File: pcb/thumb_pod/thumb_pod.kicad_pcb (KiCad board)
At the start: 2 copper layers, 60 x 56 mm, 17 parts, among them J1 Conn_02x06_Odd_Even, SW1 SW_Push, SW2 SW_Push, SW3 SW_Push, SW4 SW_Push, U1 RKJXM1015004

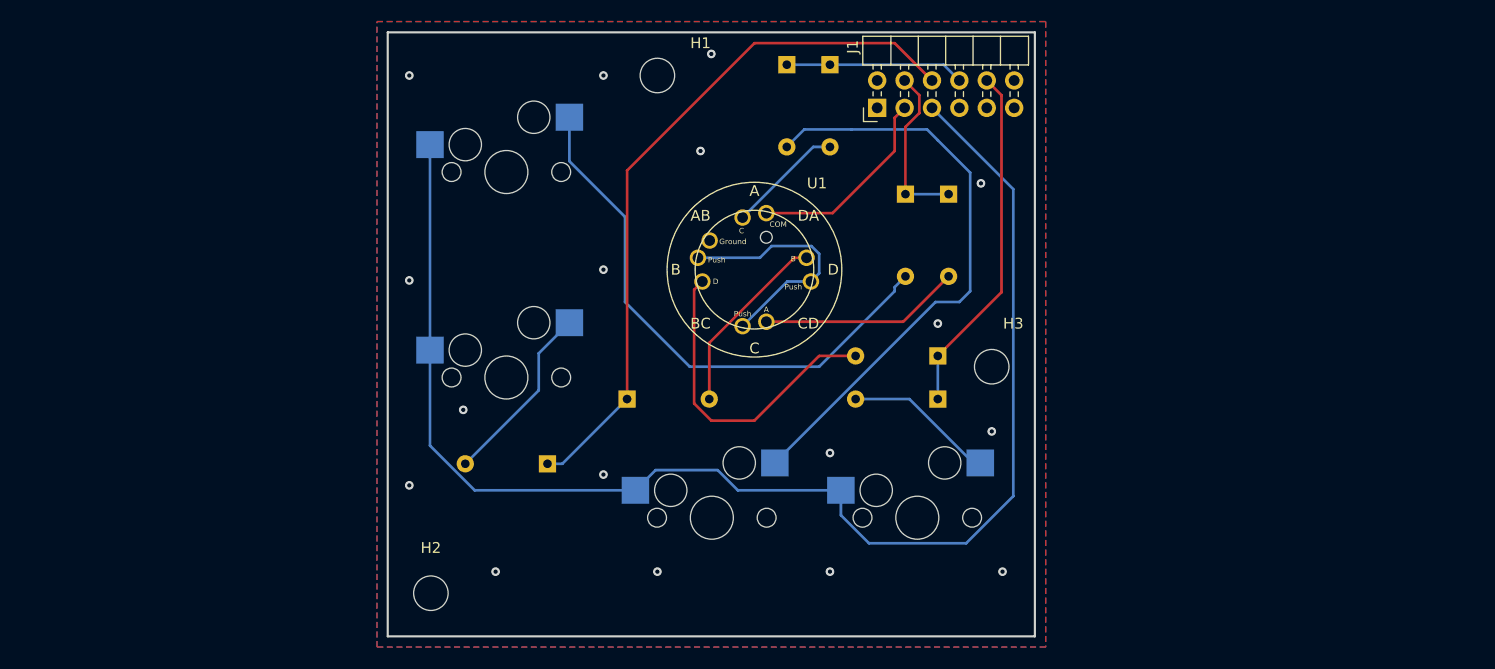
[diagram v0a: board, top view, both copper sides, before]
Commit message: - Added multiple positions for each switch to allow for tweaking
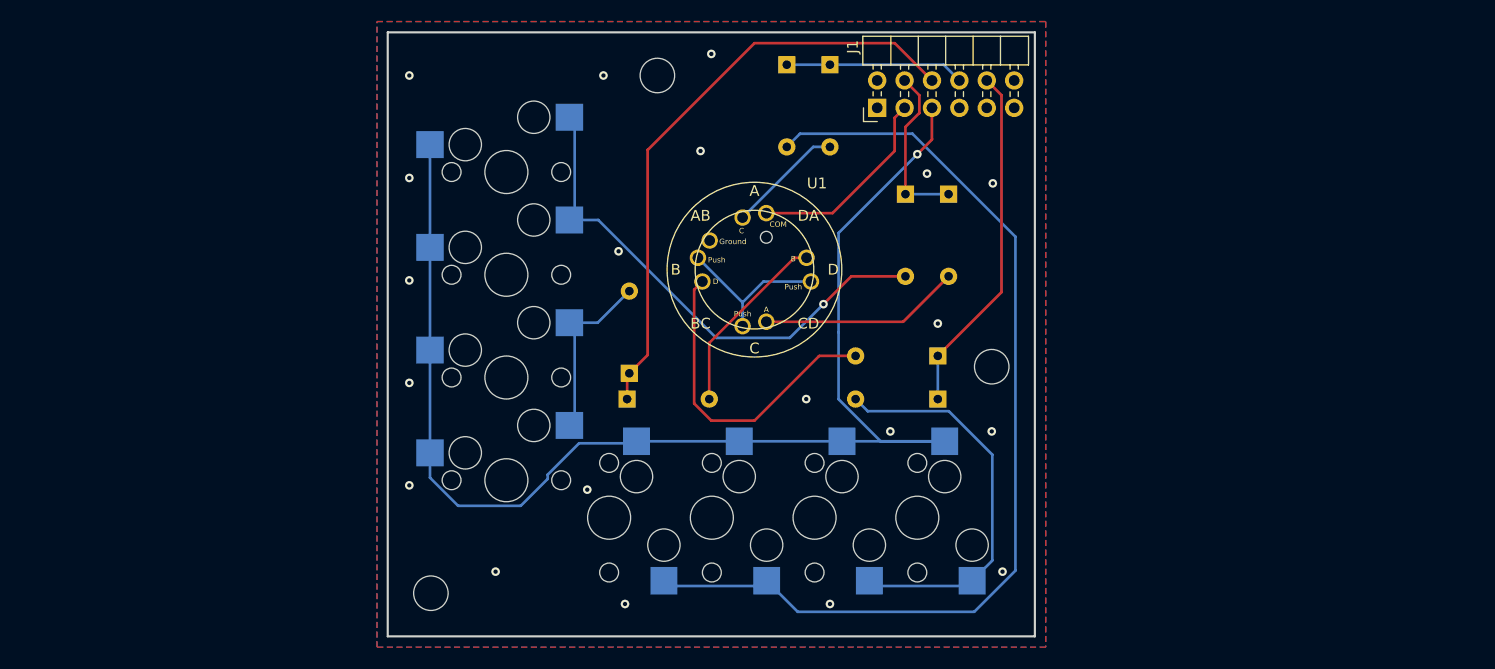
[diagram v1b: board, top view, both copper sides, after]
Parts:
- added SW5: SW_Push, keypad:MXOnly-1U-Hotswap, F.Cu at (97.0, 46.5)
- added SW6: SW_Push, keypad:MXOnly-1U-Hotswap, F.Cu at (97.0, 65.5)
- added SW7: SW_Push, keypad:MXOnly-1U-Hotswap, F.Cu at (106.5, 69.0)
- added SW8: SW_Push, keypad:MXOnly-1U-Hotswap, F.Cu at (125.6, 69.0)
- moved D4 11.3 mm to (108.4, 55.6), turned to 90 degrees
- turned SW3 to -90 degrees
- turned SW4 to -90 degrees
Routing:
- net Net-(D6-Pad2): track 55.0 -> 92.4 mm
- net Net-(D8-Pad2): track 14.0 -> 37.2 mm
- net /Col1: track 65.7 -> 55.8 mm
- net unconnected-(U1-Pad3): track 22.9 -> 15.5 mm
- net /Row5: track 129.6 -> 124.4 mm, vias 0 -> 1
- net Net-(SW1-Pad2): track 51.4 -> 48.0 mm, vias 0 -> 1
- net /GND: vias 17 -> 20

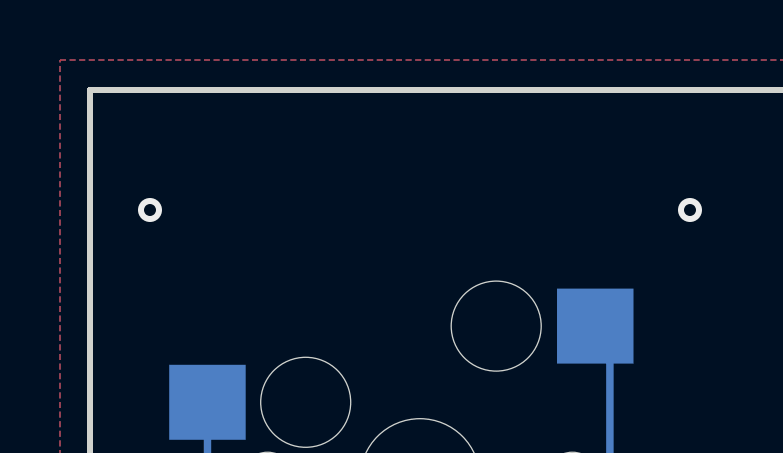
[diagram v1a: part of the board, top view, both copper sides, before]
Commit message: - Added a board label and version
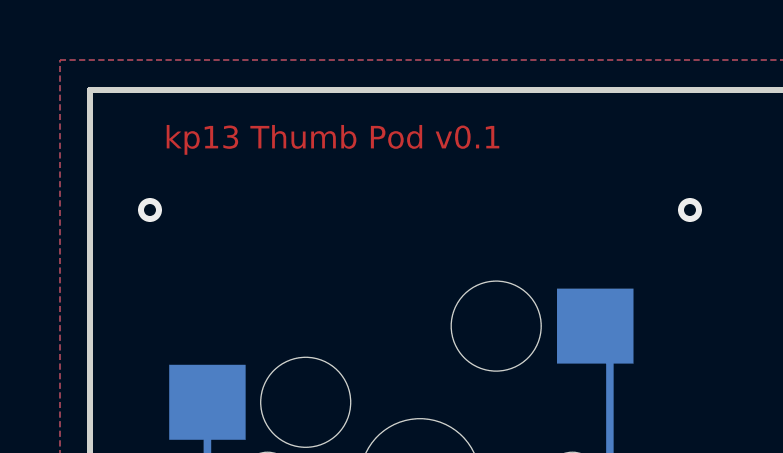
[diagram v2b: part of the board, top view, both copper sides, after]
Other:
- board text added: "kp13 Thumb Pod v0.1"
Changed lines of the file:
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@@
   (gr_line (start 146 24) (end 86 24) (layer "Edge.Cuts") (width 0.2))
   (gr_line (start 86 80) (end 146 80) (layer "Edge.Cuts") (width 0.2))
+  (gr_text "kp13 Thumb Pod v0.1" (at 94.1 25.6) (layer "F.Cu")
+    (effects (font (size 0.75 0.75) (thickness 0.1875)))
+  )
   (segment (start 135.285 29.825) (end 135.285 31.486701) (width 0.25) (layer "F.Cu") (net 1))
   (segment (start 135.285 31.486701) (end 134 32.771701) (width 0.25) (layer "F.Cu") (net 1))

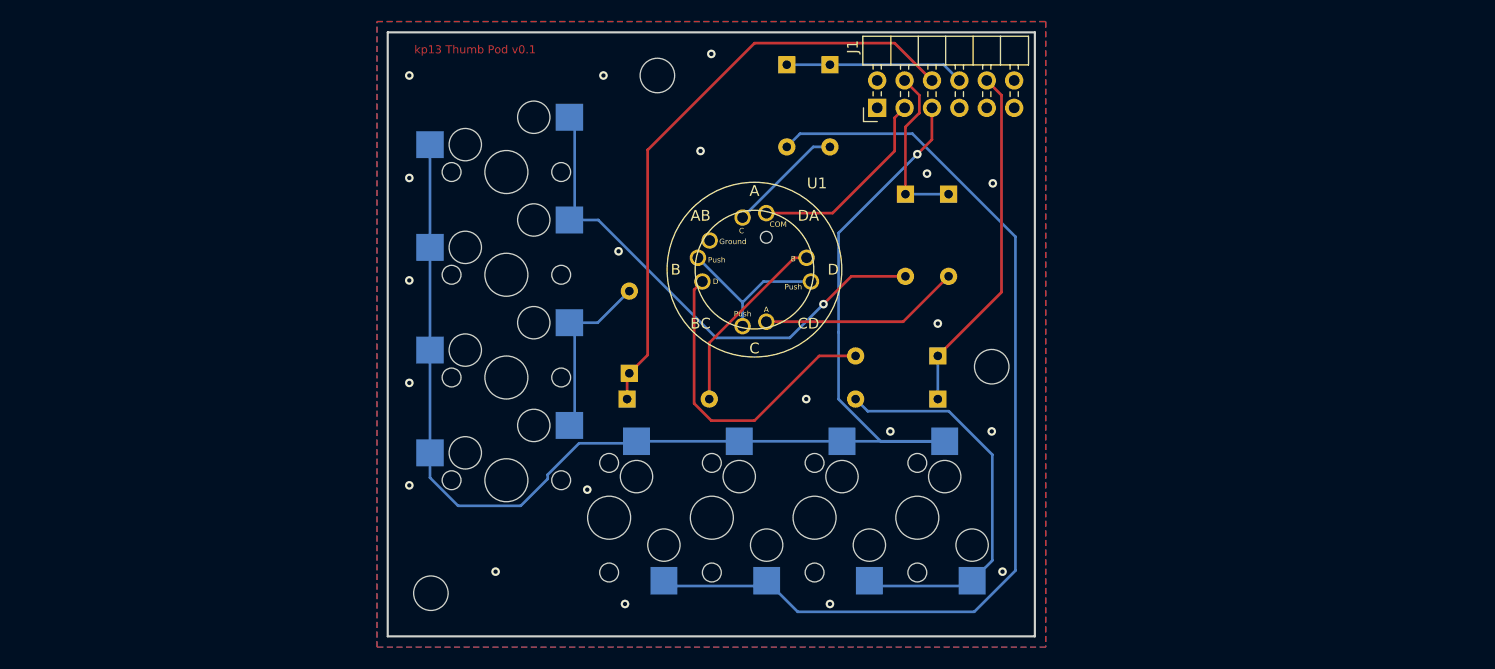
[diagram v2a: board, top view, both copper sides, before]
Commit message: - Added a preliminary "mini" thumb pod with only the directional stick  - Added mouse bite footprint from Panelization.pretty
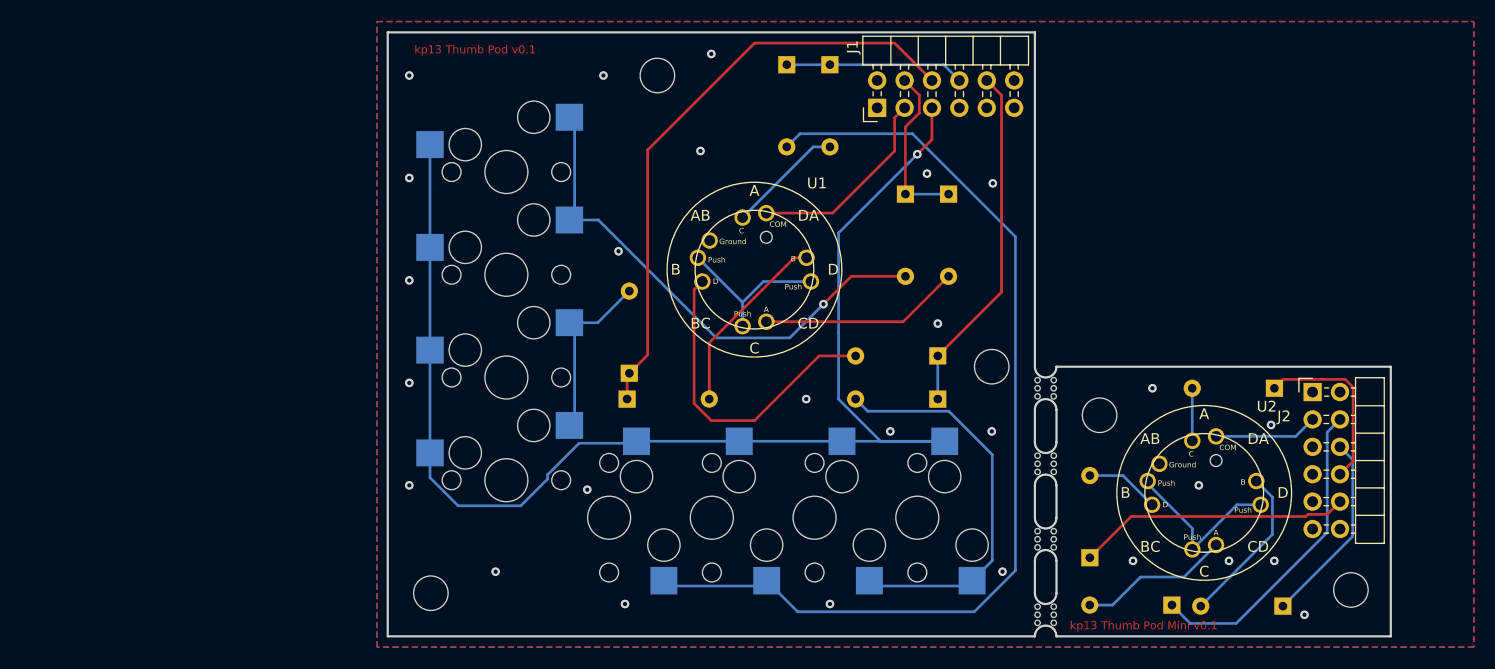
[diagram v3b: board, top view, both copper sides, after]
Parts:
- added D10: 1N4148, Diode_THT:D_DO-35_SOD27_P7.62mm_Horizontal, B.Cu at (169.0, 77.2)
- added D11: 1N4148, Diode_THT:D_DO-35_SOD27_P7.62mm_Horizontal, B.Cu at (168.2, 57.0)
- added D12: 1N4148, Diode_THT:D_DO-35_SOD27_P7.62mm_Horizontal, B.Cu at (151.1, 72.7)
- added D9: 1N4148, Diode_THT:D_DO-35_SOD27_P7.62mm_Horizontal, B.Cu at (158.7, 77.1)
- added H4: MountingHole, MountingHole:MountingHole_3.2mm_M3, F.Cu at (152.0, 59.5)
- added H5: MountingHole, MountingHole:MountingHole_3.2mm_M3, F.Cu at (175.3, 75.7)
- added J2: Conn_02x06_Odd_Even, keypad:PinHeader_2x06_P2.54mm_Horizontal, F.Cu at (171.8, 57.4)
- added U2: RKJXM1015004, thumb_pod:RKJXM1015004, F.Cu at (161.7, 66.7)
- added mouse-bite-2mm-slot: VAL**, thumb_pod:mouse-bite-2mm-slot, F.Cu at (147.0, 78.0)
- added mouse-bite-2mm-slot: VAL**, thumb_pod:mouse-bite-2mm-slot, F.Cu at (147.0, 64.0)
- added mouse-bite-2mm-slot: VAL**, thumb_pod:mouse-bite-2mm-slot, F.Cu at (147.0, 71.0)
- added mouse-bite-2mm-slot: VAL**, thumb_pod:mouse-bite-2mm-slot, F.Cu at (147.0, 57.0)
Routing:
- net /Col0: track 15.6 -> 45.2 mm
- net /Col3: track 32.6 -> 57.9 mm
- net /Col1: track 55.8 -> 73.7 mm
- net /Col2: track 16.6 -> 33.1 mm
- net unconnected-(U2-Pad3): track 0.00 -> 16.1 mm
- net Net-(D10-Pad2): track 0.00 -> 15.0 mm
- net Net-(D9-Pad2): track 0.00 -> 14.0 mm
- net /Row4: track 18.7 -> 28.3 mm
- net Net-(D12-Pad2): track 0.00 -> 6.89 mm
- net Net-(D11-Pad2): track 0.00 -> 4.87 mm
- net /GND: vias 20 -> 27
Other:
- board size 60 x 56 mm -> 93 x 56 mm
- board text added: "kp13 Thumb Pod Mini v0.1"

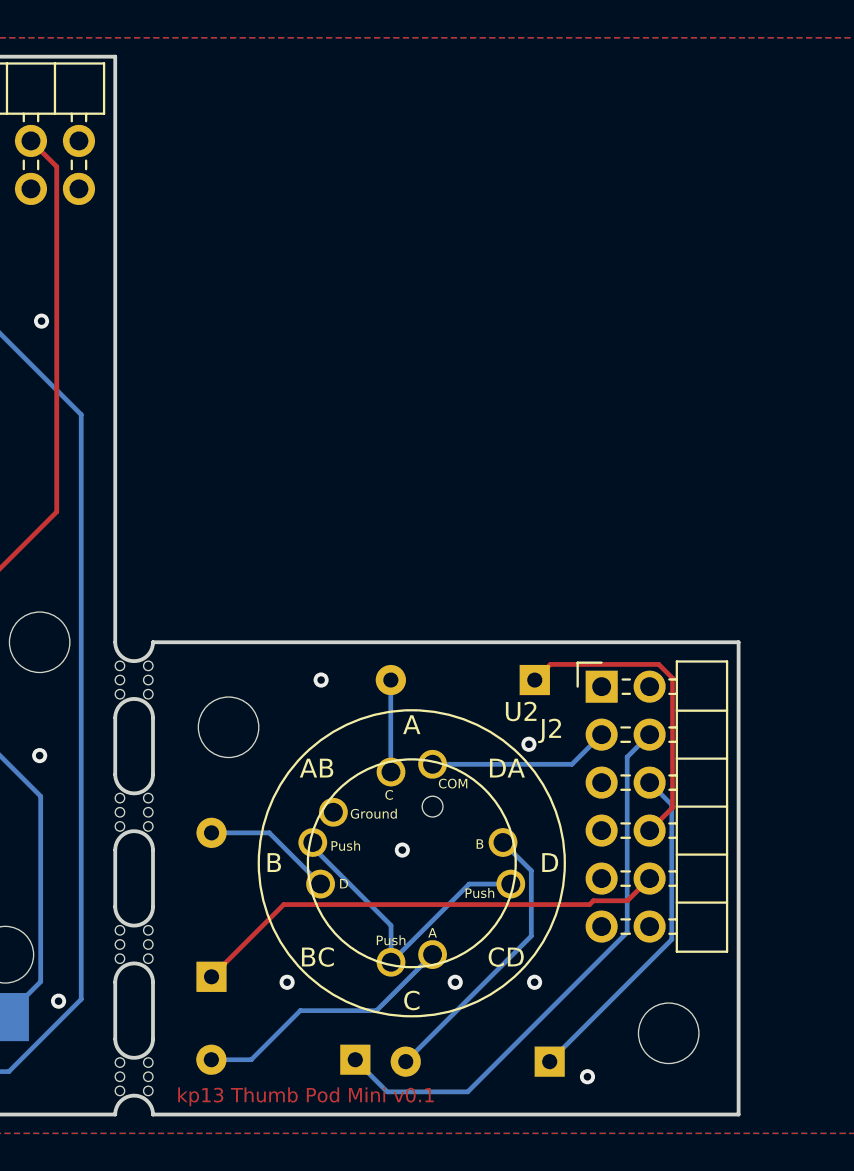
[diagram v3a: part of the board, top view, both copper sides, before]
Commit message: - Added experimental alternate layouts for the thumb pod  - Attempted some DIY panelization
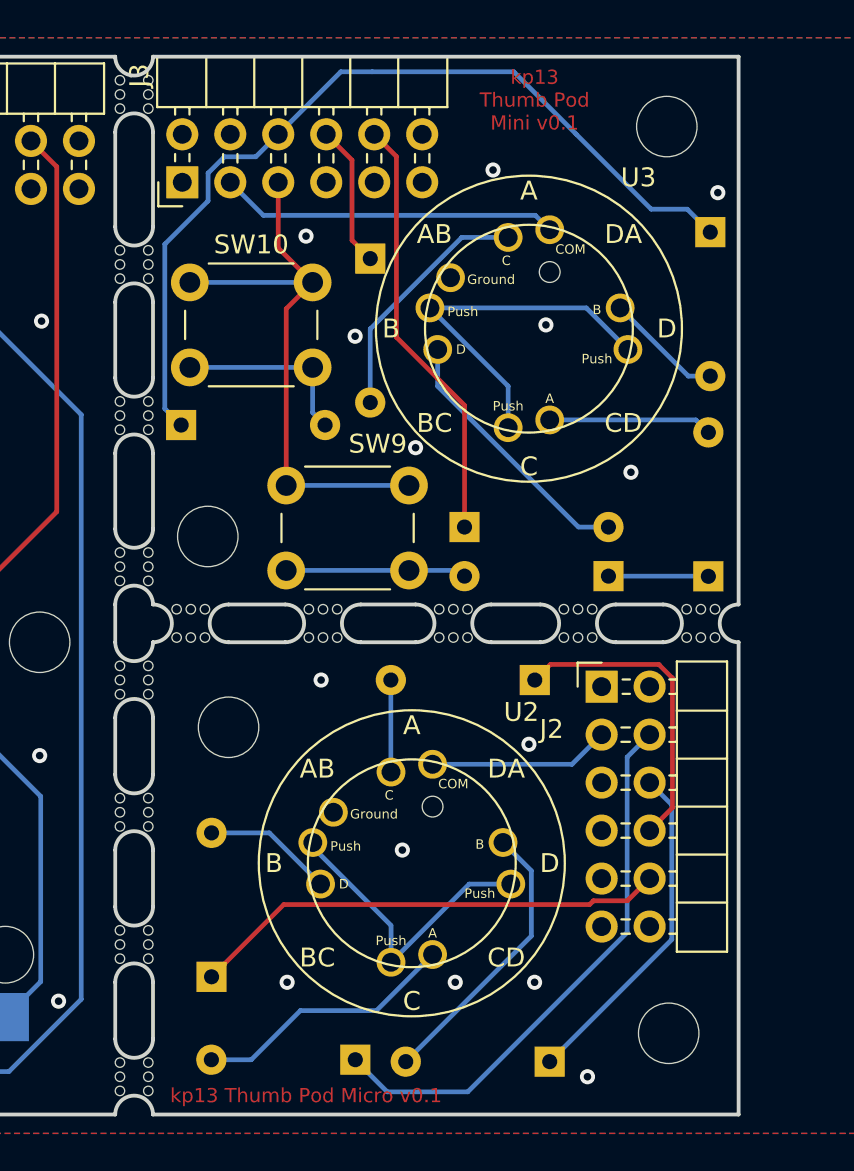
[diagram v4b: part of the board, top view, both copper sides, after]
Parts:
- added D13: 1N4148, Diode_THT:D_DO-35_SOD27_P7.62mm_Horizontal, B.Cu at (177.4, 51.5)
- added D14: 1N4148, Diode_THT:D_DO-35_SOD27_P7.62mm_Horizontal, B.Cu at (177.5, 33.3)
- added D15: 1N4148, Diode_THT:D_DO-35_SOD27_P7.62mm_Horizontal, B.Cu at (159.5, 34.7)
- added D16: 1N4148, Diode_THT:D_DO-35_SOD27_P7.62mm_Horizontal, B.Cu at (172.1, 51.5)
- added D17: 1N4148, Diode_THT:D_DO-35_SOD27_P7.62mm_Horizontal, B.Cu at (164.5, 48.9)
- added D18: 1N4148, Diode_THT:D_DO-35_SOD27_P7.62mm_Horizontal, B.Cu at (149.5, 43.5)
- added H6: MountingHole, MountingHole:MountingHole_3.2mm_M3, F.Cu at (150.9, 49.4)
- added H7: MountingHole, MountingHole:MountingHole_3.2mm_M3, F.Cu at (175.2, 27.7)
- added J3: Conn_02x06_Odd_Even, keypad:PinHeader_2x06_P2.54mm_Horizontal, F.Cu at (149.6, 30.6)
- added SW10: SW_Push, Button_Switch_THT:SW_PUSH_6mm, F.Cu at (149.9, 36.0)
- added SW9: SW_Push, Button_Switch_THT:SW_PUSH_6mm, F.Cu at (155.1, 46.7)
- added U3: RKJXM1015004, thumb_pod:RKJXM1015004, F.Cu at (167.9, 38.4)
- added mouse-bite-2mm-slot: VAL**, thumb_pod:mouse-bite-2mm-slot, F.Cu at (177.0, 54.0)
- added mouse-bite-2mm-slot: VAL**, thumb_pod:mouse-bite-2mm-slot, F.Cu at (147.0, 35.0)
- added mouse-bite-2mm-slot: VAL**, thumb_pod:mouse-bite-2mm-slot, F.Cu at (170.5, 54.0)
- added mouse-bite-2mm-slot: VAL**, thumb_pod:mouse-bite-2mm-slot, F.Cu at (163.9, 54.0)
- added mouse-bite-2mm-slot: VAL**, thumb_pod:mouse-bite-2mm-slot, F.Cu at (147.0, 43.0)
- added mouse-bite-2mm-slot: VAL**, thumb_pod:mouse-bite-2mm-slot, F.Cu at (157.0, 54.0)
- added mouse-bite-2mm-slot: VAL**, thumb_pod:mouse-bite-2mm-slot, F.Cu at (147.0, 51.0)
- added mouse-bite-2mm-slot: VAL**, thumb_pod:mouse-bite-2mm-slot, F.Cu at (150.0, 54.0)
- added mouse-bite-2mm-slot: VAL**, thumb_pod:mouse-bite-2mm-slot, F.Cu at (147.0, 26.0)
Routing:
- net /Col1: track 73.7 -> 120.7 mm
- net /Row5: track 124.4 -> 154.8 mm
- net /Col3: track 57.9 -> 80.7 mm
- net unconnected-(U3-Pad3): track 0.00 -> 19.4 mm
- net /Row4: track 28.3 -> 46.2 mm
- net Net-(D17-Pad2): track 0.00 -> 14.1 mm
- net Net-(D15-Pad2): track 0.00 -> 13.2 mm
- net Net-(D18-Pad2): track 0.00 -> 9.82 mm
- net Net-(D16-Pad2): track 0.00 -> 9.56 mm
- net Net-(D13-Pad2): track 0.00 -> 8.67 mm
- net /Col2: track 33.1 -> 40.7 mm
- net Net-(D14-Pad2): track 0.00 -> 6.27 mm
- net /Col0: track 45.2 -> 50.5 mm
- net /GND: vias 27 -> 34
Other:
- outline, holes or cut-outs redrawn
- board text added: "kp13 Thumb Pod Micro v0.1"
